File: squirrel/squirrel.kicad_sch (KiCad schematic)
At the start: 69 parts, among them J1 Conn_01x01, J10 Conn_01x01, J11 Conn_01x01, J12 Conn_01x01, J13 Conn_01x01, J14 Conn_01x01, J15 Conn_01x01, J16 Conn_01x01, J17 Conn_01x01, J18 Conn_01x01, J19 Conn_01x01, J2 Conn_01x01, J20 Conn_01x01, J21 Conn_01x01, J22 Conn_01x01, J23 Conn_01x01, J24 Conn_01x01, J25 Conn_01x01, J26 Conn_01x01, J27 Conn_01x01, J28 Conn_01x01, J29 Conn_01x01, J3 Conn_01x01, J30 Conn_01x01, J31 Conn_01x01, J32 Conn_01x01, J33 Conn_01x01, J34 Conn_01x01, J35 Conn_01x01, J36 Conn_01x01, J37 Conn_01x01, J38 Conn_01x01, J39 Conn_01x01, J4 Conn_01x01, J40 Conn_01x01, J41 Conn_02x20_Odd_Even, J42 Conn_01x02, J43 Conn_02x20_Odd_Even, J44 Conn_02x25_Odd_Even, J5 Conn_01x01, J6 Conn_01x01, J7 Conn_01x01, J8 Conn_01x01, J9 Conn_01x01

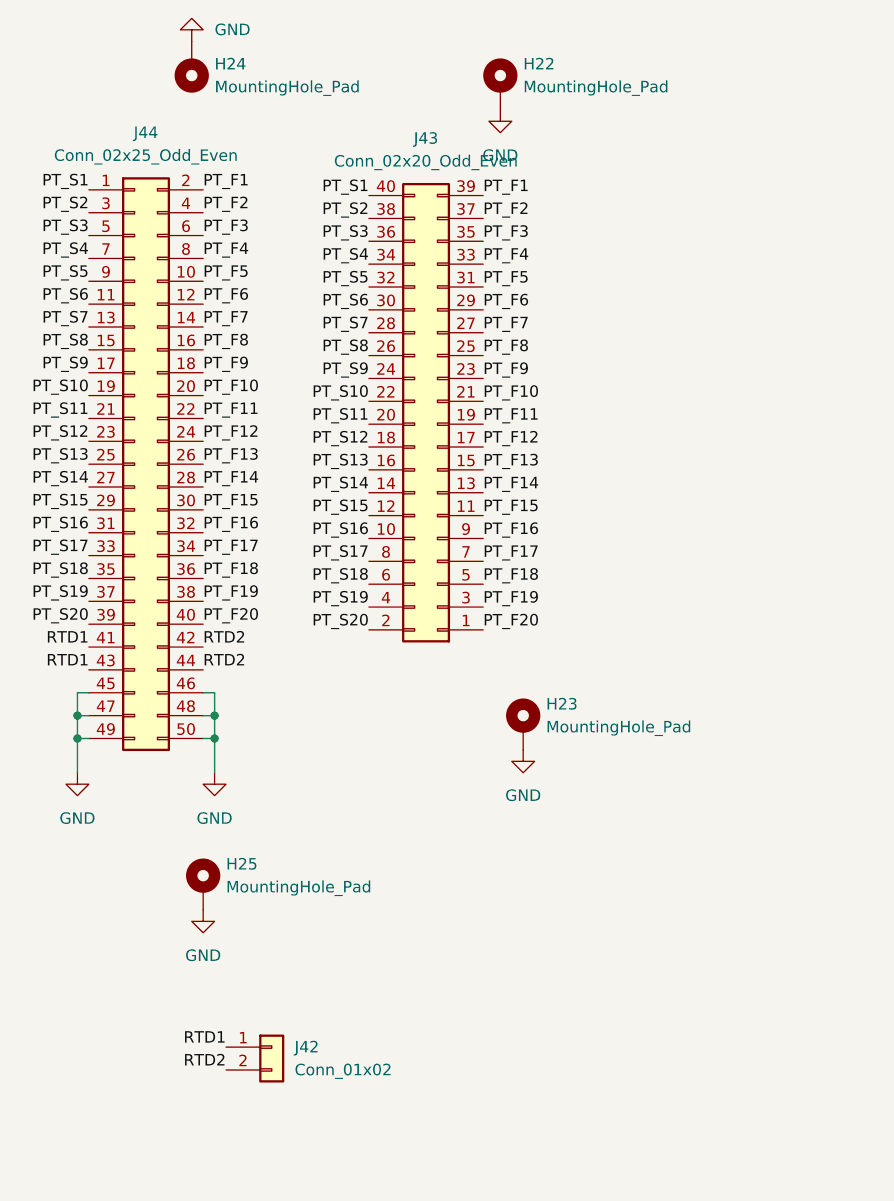
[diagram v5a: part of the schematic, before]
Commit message: smaller pt pcb
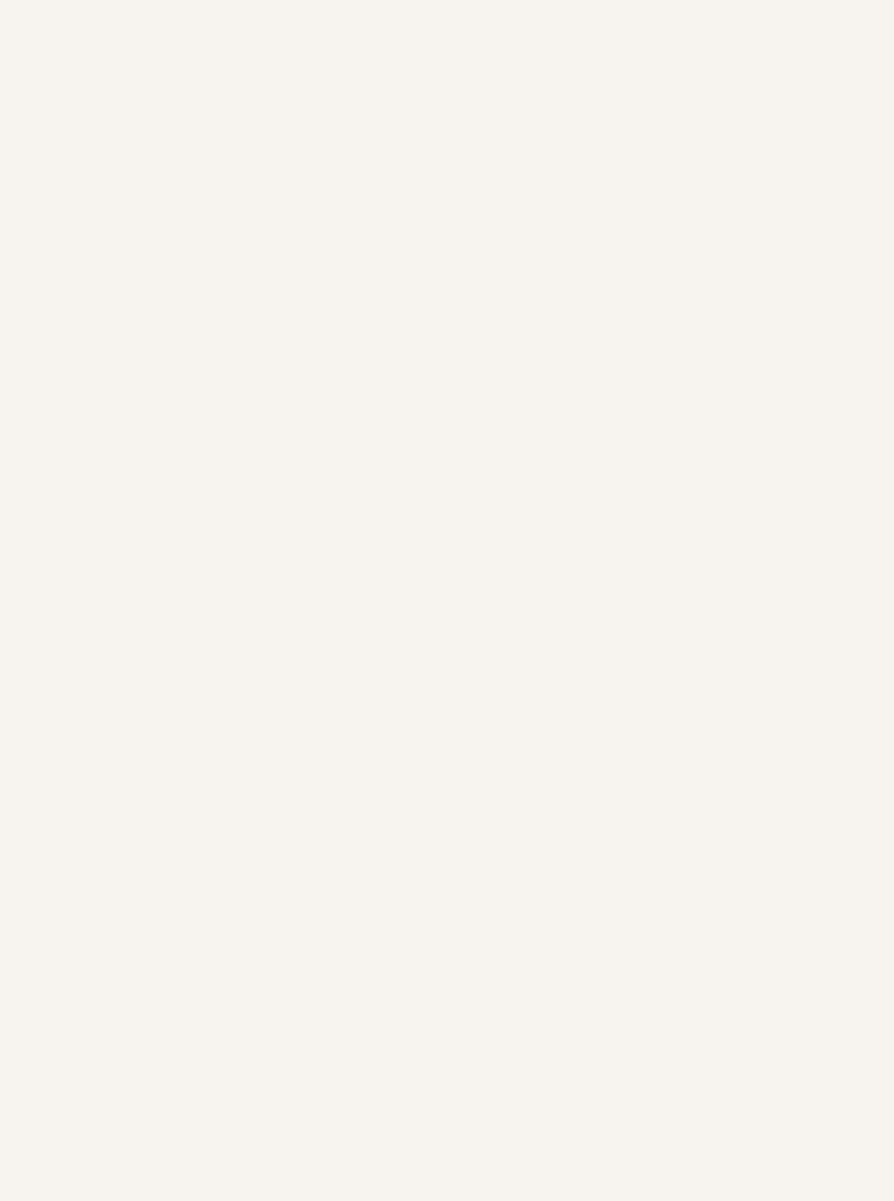
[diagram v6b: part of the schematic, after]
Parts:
- removed H22, H23, H24, H25: MountingHole_Pad, custom_footprints:MountingHole_3.2mm_M3_ISO7380_Pad_TopBottom_screw, symbol Mechanical:MountingHole_Pad
- removed J42: Conn_01x02, Connector_Wire:SolderWire-0.1sqmm_1x02_P3.6mm_D0.4mm_OD1mm, symbol Connector_Generic:Conn_01x02
- removed J43: Conn_02x20_Odd_Even, custom_footprints:TST-120-01-G-D, symbol Connector_Generic:Conn_02x20_Odd_Even
- removed J44: Conn_02x25_Odd_Even, custom_footprints:TST-125-01-G-D, symbol Connector_Generic:Conn_02x25_Odd_Even

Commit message: silk
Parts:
- added LOGO1, LOGO2: Logo_Open_Hardware_Small, custom_footprints:site_small, symbol Graphic:Logo_Open_Hardware_Small
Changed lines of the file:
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@@
     (pin "1")
+  )
+  (symbol (lib_id "Graphic:Logo_Open_Hardware_Small") (at 185.42 175.26 0) (unit 1)
+    (in_bom yes) (on_board yes) (fields_autoplaced)
+    (property "Reference" "LOGO1" (id 0) (at 185.42 168.275 0)
+      (effects (font (size 1.27 1.27)) hide)
+    )
+    (property "Value" "Logo_Open_Hardware_Small" (id 1) (at 185.42 180.975 0)
+      (effects (font (size 1.27 1.27)) hide)
+    )
+    (property "Footprint" "custom_footprints:site_small" (id 2) (at 185.42 175.26 0)
+      (effects (font (size 1.27 1.27)) hide)
+    )
+    (property "Datasheet" "~" (id 3) (at 185.42 175.26 0)
+      (effects (font (size 1.27 1.27)) hide)
+    )
   )
   (symbol (lib_id "Mechanical:MountingHole") (at 142.875 104.775 90) (unit 1)
@@
     )
   )
+  (symbol (lib_id "Graphic:Logo_Open_Hardware_Small") (at 276.86 173.99 0) (unit 1)
+    (in_bom yes) (on_board yes) (fields_autoplaced)
+    (property "Reference" "LOGO2" (id 0) (at 276.86 167.005 0)
+      (effects (font (size 1.27 1.27)) hide)
+    )
+    (property "Value" "Logo_Open_Hardware_Small" (id 1) (at 276.86 179.705 0)
+      (effects (font (size 1.27 1.27)) hide)
+    )
+    (property "Footprint" "custom_footprints:site_small" (id 2) (at 276.86 173.99 0)
+      (effects (font (size 1.27 1.27)) hide)
+    )
+    (property "Datasheet" "~" (id 3) (at 276.86 173.99 0)
+      (effects (font (size 1.27 1.27)) hide)
+    )
+  )
   (symbol (lib_id "Mechanical:MountingHole") (at 218.44 71.755 90) (unit 1)
     (in_bom yes) (on_board yes) (fields_autoplaced)
@@
       (reference "J41") (unit 1) (value "Conn_02x20_Odd_Even") (footprint "custom_footprints:TST-120-01-G-D")
     )
-  )
+    (path "/2d079211-de1e-4d0f-bf0f-00f124f0ca69"
+      (reference "LOGO1") (unit 1) (value "Logo_Open_Hardware_Small") (footprint "custom_footprints:site_small")
+    )
+    (path "/efd2b263-faa2-48bc-b10c-0bcd2a1f670e"
+      (reference "LOGO2") (unit 1) (value "Logo_Open_Hardware_Small") (footprint "custom_footprints:site_small")
+    )
+  )
